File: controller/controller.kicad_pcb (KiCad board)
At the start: 4 copper layers, 93 x 39 mm, 132 parts, among them J1 Conn_01x14, J2 Conn_01x14, J3 Conn_01x14, J4 Conn_01x14, J5 Conn_01x14, J6 USB_C_Receptacle_USB2.0_16P, J7 USB_C_Receptacle_USB2.0_16P, J8 GRPB072VWQS-RC, J9 Conn_01x03_Pin, U1 STM32G474RCTx, U10 PI5C3257, U11 QSBT40-7-F, U12 QSBT40-7-F, U13 QSBT40-7-F, U2 LM5168, U3 TLV76133DCY, U4 TLV76150DCY, U5 ECMF02-2AMX6, U6 ESP32-C6-WROOM-1, U7 ECMF02-2AMX6, U8 PI5C3257, U9 PY32F002AA15M

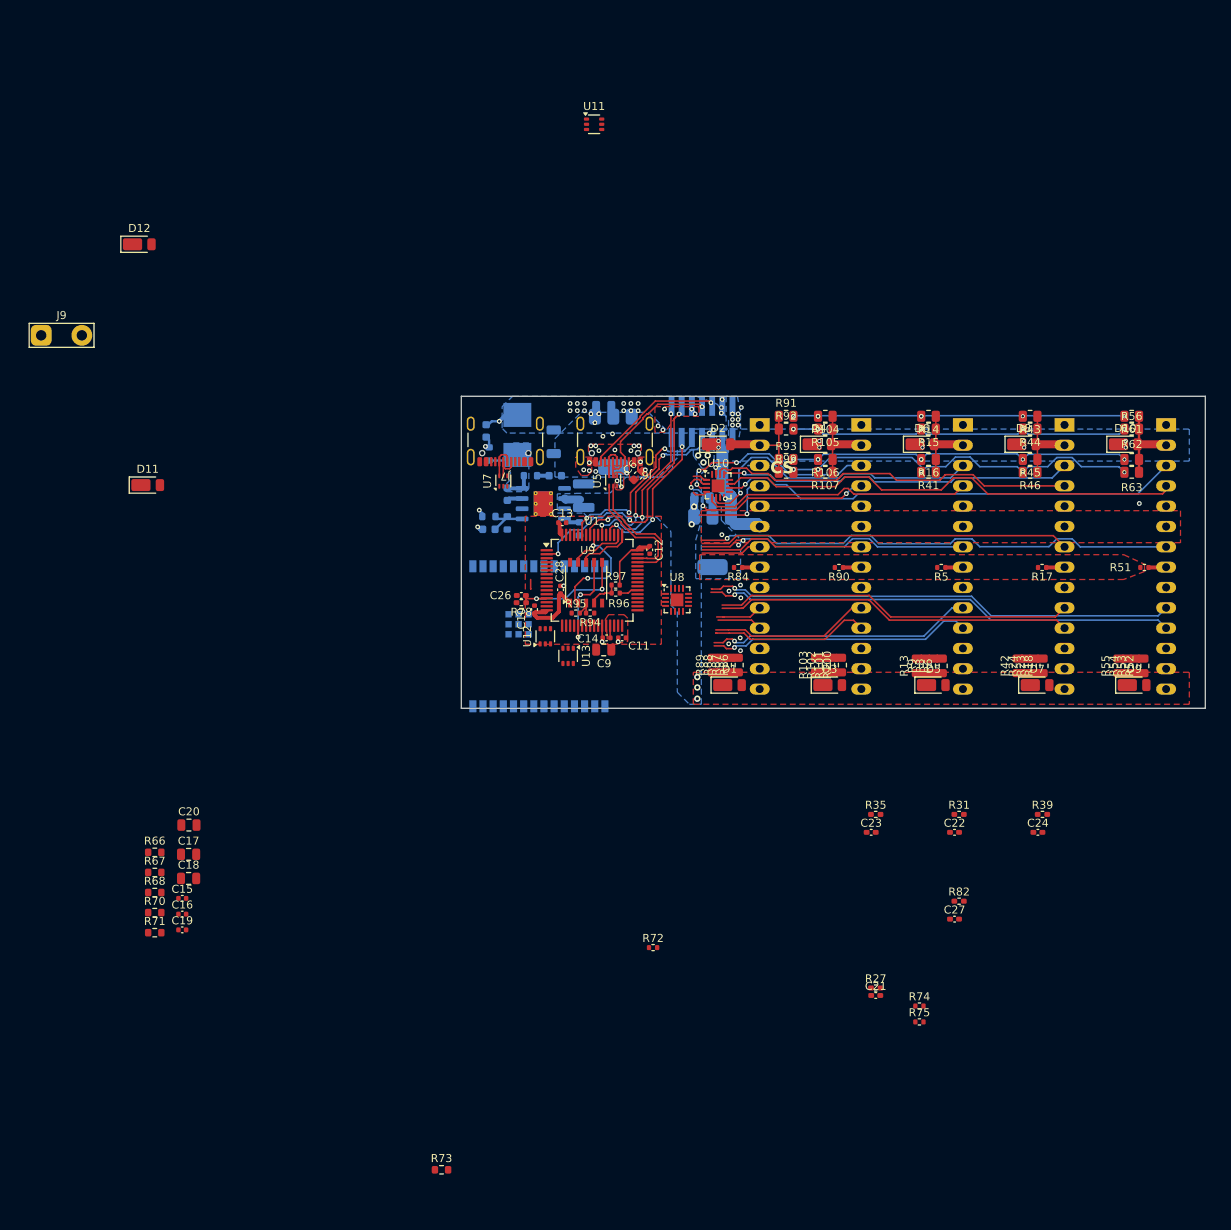
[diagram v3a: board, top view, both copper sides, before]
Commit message: Controller move DC/DC to between HB4 and HB5
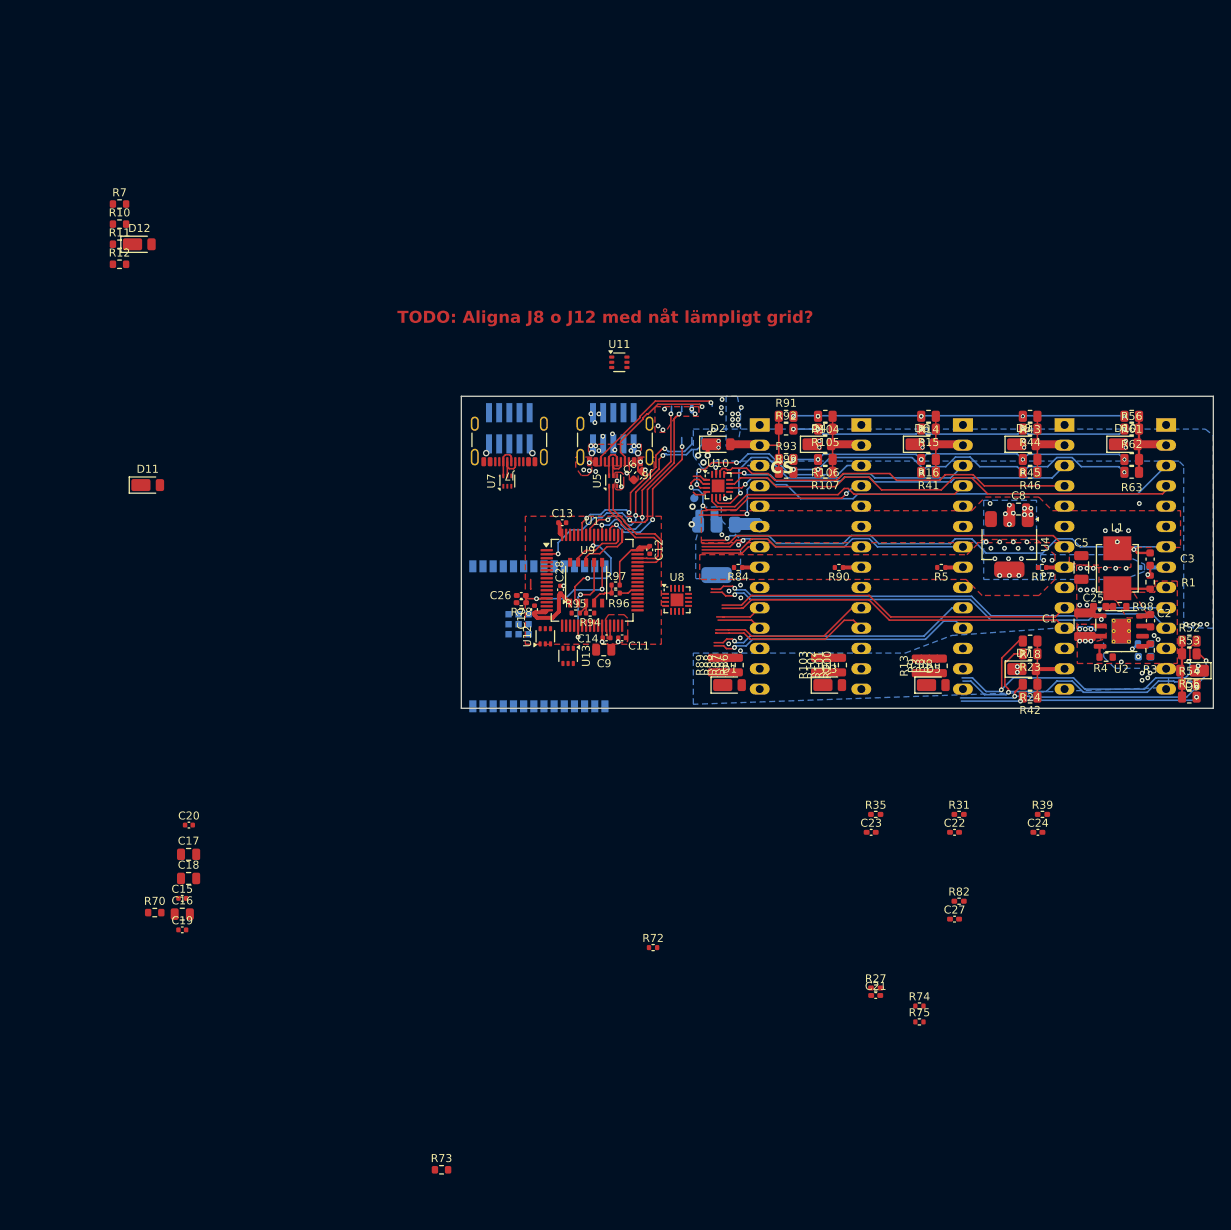
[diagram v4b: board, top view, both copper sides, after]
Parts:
- removed J9: Conn_01x03_Pin, TestPoint:TestPoint_2Pads_Pitch5.08mm_Drill1.3mm
- removed R66, R67, R68: 10k, Resistor_SMD:R_0603_1608Metric
- removed R71: 1k, Resistor_SMD:R_0603_1608Metric
- added J12: GRPB072VWQS-RC, Connector_PinHeader_1.27mm:PinHeader_2x05_P1.27mm_Vertical_SMD, B.Cu at (83.0, 69.0)
- added R10: 10k, Resistor_SMD:R_0603_1608Metric, F.Cu at (34.3, 43.5)
- added R11: 10k, Resistor_SMD:R_0603_1608Metric, F.Cu at (34.3, 46.0)
- added R12: 1k, Resistor_SMD:R_0603_1608Metric, F.Cu at (34.3, 48.5)
- added R7: 10k, Resistor_SMD:R_0603_1608Metric, F.Cu at (34.3, 41.0)
- C1, C2, C25, C3, C5, C8, R1, R3, R4, R98, U4: moved to F.Cu
- C16: value 100nF -> 10uF; footprint Capacitor_SMD:C_0402_1005Metric -> Capacitor_SMD:C_0805_2012Metric
- C20: value 10uF -> 100nF; footprint Capacitor_SMD:C_0805_2012Metric -> Capacitor_SMD:C_0402_1005Metric
- J8: footprint Connector_PinHeader_1.27mm:PinHeader_2x07_P1.27mm_Vertical_SMD -> Connector_PinHeader_1.27mm:PinHeader_2x05_P1.27mm_Vertical_SMD
- L1: value 180uH 630mOhm, duger LQH55DN151M03L? -> duger CLF7045NIT-151M-D?; moved to F.Cu
- R51: moved to B.Cu
- U2: value LM5168 -> LM5169PDDAR; moved to F.Cu
- moved C3 84.5 mm to (163.1, 85.4)
- moved R1 84.2 mm to (163.1, 88.2)
- moved C4 83.5 mm to (162.4, 97.6)
- moved R2 83.5 mm to (162.4, 96.0)
- moved C2 81.9 mm to (163.2, 93.1)
- moved R3 81.9 mm to (163.1, 96.8)
- moved L1 76.8 mm to (159.0, 86.5)
- moved R98 75.5 mm to (159.3, 91.3), turned to 180 degrees
- moved U2 74.0 mm to (159.5, 94.4), turned to 0 degrees
- moved C25 70.0 mm to (156.8, 91.3), turned to 180 degrees
- moved C5 67.8 mm to (154.5, 86.4)
- moved R4 67.8 mm to (157.6, 97.6), turned to 0 degrees
- moved C1 64.7 mm to (154.9, 93.6)
- moved C8 39.6 mm to (146.7, 79.1), turned to 0 degrees
- moved U4 37.1 mm to (145.5, 83.5)
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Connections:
- net ESP_USB_D+ renamed /ESP_USB_D+
- net ESP_USB_D- renamed /ESP_USB_D-
- net Net-(D11-A) renamed /VBUS1
- net Net-(D12-A) renamed /VBUS2
- C15 pad 1: Net-(U6-EN/CHIP_PU) -> +3V3
- C20 pad 1: +3V3 -> Net-(U6-EN/CHIP_PU)
- J8 pad 10: +3V3 -> 6-18V
- J8 pad 3: 6-18V -> Earth
- J8 pad 7: /CC2_MCU -> Earth
- J8 pad 9: /CC1_MCU -> +3V3
- U2 pad 6: unconnected-(U2-PGOOD-Pad6) -> Earth
- U6 pad 18: /STM32_BOOT0 -> /STM32_NRST_TO_ESP
- U6 pad 19: /STM32_NRST_TO_ESP -> /STM32_BOOT0
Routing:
- net FB_A_FULL: track 58.2 -> 101.8 mm, vias 7 -> 9
- net FB_B_FULL: track 55.2 -> 98.5 mm, vias 7 -> 9
- net FB_C_FULL: track 43.0 -> 75.1 mm, vias 5 -> 7
- net FB_D_FULL: track 46.3 -> 76.2 mm, vias 5 -> 7
- net /hb-card4/FB_x_FULL_HI: track 0.08 -> 10.7 mm
- net 6-18V: track 30.8 -> 21.0 mm, vias 14 -> 10
- net /hb-card5/FB_x_FULL_HI: track 0.08 -> 7.08 mm
- net Net-(U2-FB): track 5.66 -> 0.00 mm
- net Net-(U2-SW): track 7.37 -> 4.12 mm
- net +5V: track 2.49 -> 0.00 mm, vias 0 -> 22
- net Net-(U2-BST): track 1.94 -> 0.00 mm
- net Net-(C3-Pad2): track 13.9 -> 12.4 mm
- net Earth: track 5.22 -> 3.72 mm, vias 34 -> 46
- net Logic DC/DC in: track 2.99 -> 1.89 mm, vias 16 -> 31
- net Net-(U2-RON): track 2.04 -> 1.37 mm
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- added copper zone on In2.Cu, net Logic DC/DC in
- added copper zone on F.Cu, net Net-(U2-SW)
- removed copper zone on B.Cu, net 6-18V
- removed copper zone on In2.Cu, net 6-18V
- removed copper zone on B.Cu, net Net-(U2-SW)
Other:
- board size 93 x 39 mm -> 94 x 39 mm
- board text added: "TODO: Aligna J8 o J12 med nåt lämpligt grid?"
- board text added: "USB PD expansion PCB"

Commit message: Controller - Some smaller changes, add 3d models etc
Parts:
- added J9: GRPB072VWQS-RC, Connector_PinHeader_1.27mm:PinHeader_2x05_P1.27mm_Vertical_SMD, B.Cu at (104.7, 69.0)
- C15, C16, C17, C18: moved to B.Cu
- moved R73 74.7 mm to (83.4, 87.5)
- moved D12 69.9 mm to (102.4, 69.9), turned to -90 degrees
- moved C16 61.4 mm to (82.7, 83.6)
- moved R75 59.3 mm to (95.6, 98.2), turned to 180 degrees
- moved C18 59.1 mm to (82.7, 81.6)
- moved R74 57.1 mm to (95.6, 99.2), turned to 180 degrees
- moved C15 57.1 mm to (79.0, 84.2), turned to 180 degrees
- moved C17 53.8 mm to (79.2, 82.6), turned to 180 degrees
- moved D11 52.3 mm to (89.6, 69.2), turned to -90 degrees
- moved R12 50.5 mm to (64.6, 88.9)
- moved R7 50.5 mm to (64.6, 81.4)
- moved R10 50.5 mm to (64.6, 83.9)
- moved R11 50.5 mm to (64.6, 86.4)
- moved R72 44.8 mm to (101.3, 89.1), turned to -90 degrees
- moved R27 21.4 mm to (137.6, 119.5)
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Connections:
- net /HI_4 renamed HI_4
- net /HI_5 renamed HI_5
- net /LI_4 renamed LI_4
- net /LI_5 renamed LI_5
- J7 pad A5: unconnected-(J7-CC1-PadA5) -> /OTHER_USB_CC1
- J7 pad B5: unconnected-(J7-CC2-PadB5) -> /OTHER_USB_CC2
- U1 pad 10: Net-(U1-PC2) -> /PC2
- U1 pad 11: ADC12_IN9 -> /NTC_2
- U1 pad 22: /NTC_5 -> unconnected-(U1-PC4-Pad22)
- U1 pad 26: ADC2_IN12 -> /PB2
- U1 pad 5: /NTC_2 -> /NTC_4
- U1 pad 53: unconnected-(U1-PC11-Pad53) -> /PC11
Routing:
- net /STM32_TX: track 13.6 -> 28.1 mm, vias 2 -> 3
- net /STM32_RX: track 0.00 -> 12.8 mm, vias 0 -> 1
- net /CC2: track 17.9 -> 7.52 mm, vias 1 -> 0
- net /CC1: track 15.7 -> 6.73 mm, vias 3 -> 0
- net /~{EN_CC}: track 32.1 -> 23.8 mm, vias 3 -> 2
- net +3V3: track 20.1 -> 27.5 mm
- net /PA4: track 0.00 -> 7.11 mm
- net /CC2_MCU: track 23.9 -> 16.8 mm, vias 3 -> 2
- net /FRS: track 23.6 -> 16.7 mm, vias 3 -> 2
- net /CC1_MCU: track 22.9 -> 16.7 mm, vias 3 -> 2
- net /PA5: track 0.00 -> 4.79 mm
- net /~{EN_VCONN}: track 19.2 -> 16.4 mm, vias 3 -> 2
- net /hb-card5/FB_x_FULL_HI: track 7.08 -> 8.87 mm
- net Earth: vias 46 -> 53
- net /VBUS1: vias 17 -> 14

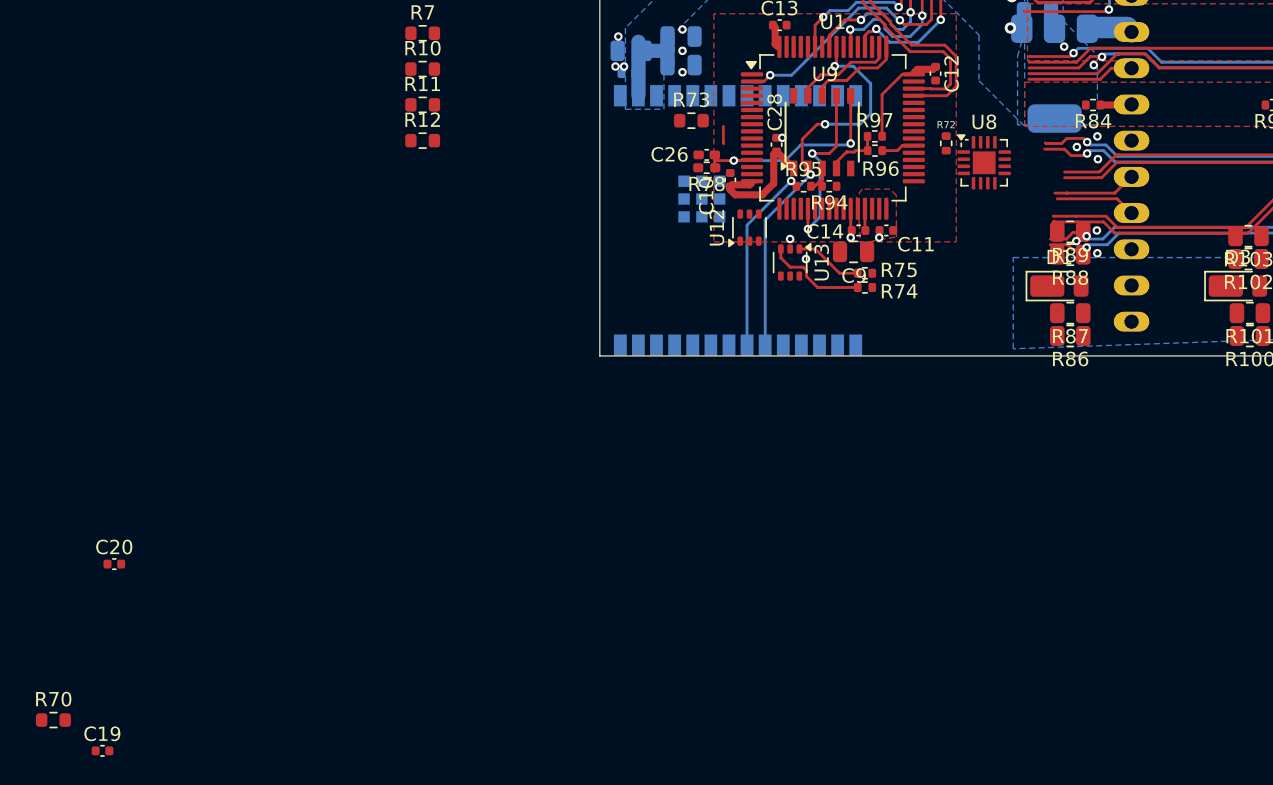
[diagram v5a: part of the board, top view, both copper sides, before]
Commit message: Controller and firwmare most pins in sync
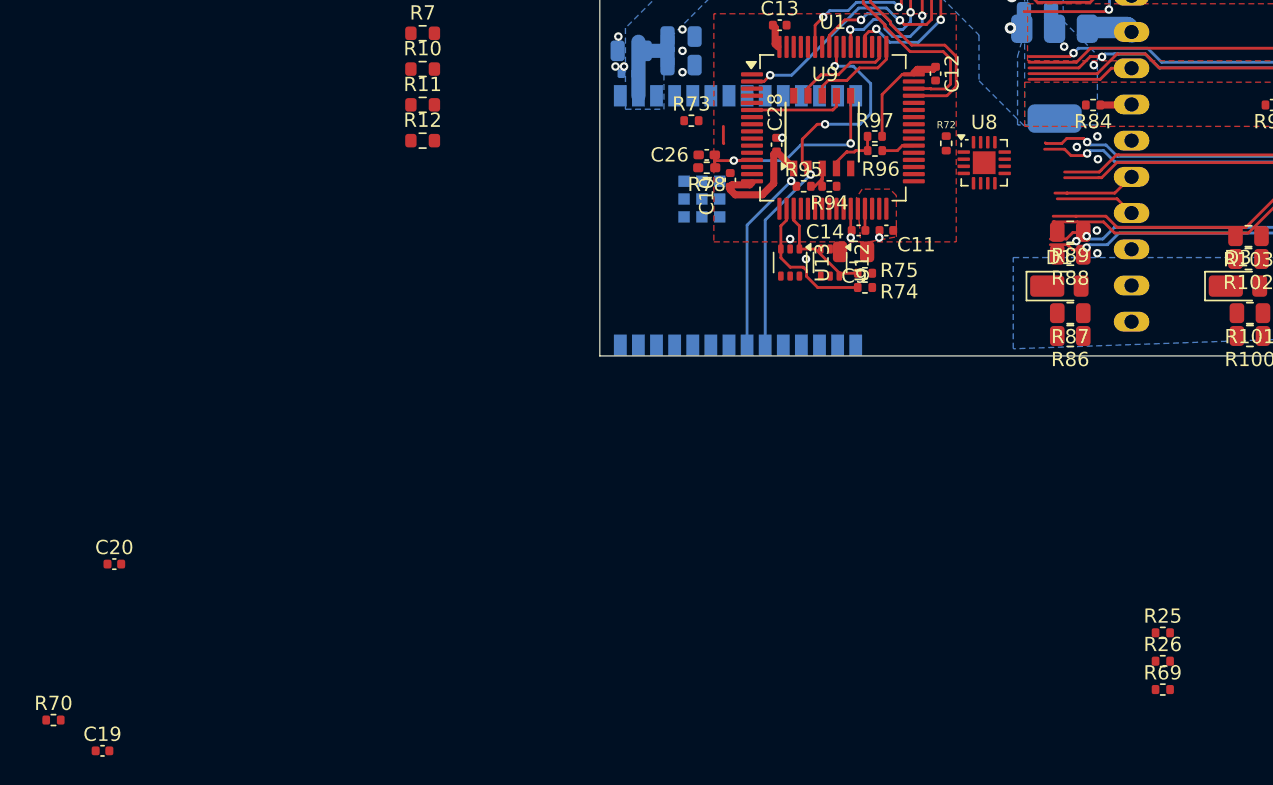
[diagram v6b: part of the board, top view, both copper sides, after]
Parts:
- added R25: 0R, Resistor_SMD:R_0402_1005Metric, F.Cu at (116.5, 123.4)
- added R26: 0R, Resistor_SMD:R_0402_1005Metric, F.Cu at (116.5, 125.4)
- added R69: 10k, Resistor_SMD:R_0402_1005Metric, F.Cu at (116.5, 127.4)
- R70, R73: footprint Resistor_SMD:R_0603_1608Metric -> Resistor_SMD:R_0402_1005Metric
- moved U12 6.16 mm to (93.2, 97.5), turned to -90 degrees
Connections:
- net HRTIM1_EEV3 renamed /pwm_led2
- net HRTIM1_EEV5 renamed /pwm_led3
- net HRTIM1_EEV6 renamed /pwm_led1
- net HRTIM1_FLT3 renamed /pwm_led4
- U1 pad 13: FB_A_FULL -> /Current_sense_4
- U1 pad 17: /Current_sense_1B -> /pwm_led5 pot2
- U1 pad 21: FB_B_FULL -> /Current_sense_5
- U1 pad 22: unconnected-(U1-PC4-Pad22) -> FB_D_FULL
- U1 pad 25: /Current_sense_3 -> /pwm_led6 pot3
- U1 pad 33: /Current_sense_? -> /Current_sense_2
- U1 pad 36: /Current_sense_2 -> /Current_sense_3
- U1 pad 6: ADC2_IN10 -> FB_B_FULL
- U1 pad 9: FB_D_FULL -> /Current_sense_1B
- U8 pad 10: LI_5 -> LI_4
- U8 pad 13: HI_5 -> HI_4
- U8 pad 3: HI_4 -> HI_5
- U8 pad 6: LI_4 -> LI_5
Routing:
- net FB_B_FULL: track 98.9 -> 93.0 mm, vias 9 -> 7
- net /PA5: track 4.79 -> 7.78 mm
- net /PA4: track 7.11 -> 10.1 mm

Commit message: Controller - some more changes
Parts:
- added C29: 10nF, Capacitor_SMD:C_0402_1005Metric, F.Cu at (132.6, 158.9)
- added C30: 10nF, Capacitor_SMD:C_0402_1005Metric, F.Cu at (132.6, 160.9)
- added C31: 10nF, Capacitor_SMD:C_0402_1005Metric, F.Cu at (132.6, 162.9)
- added C32: 10nF, Capacitor_SMD:C_0402_1005Metric, F.Cu at (132.6, 164.8)
- added C33: 10nF, Capacitor_SMD:C_0402_1005Metric, F.Cu at (123.7, 151.0)
- added C34: 10nF, Capacitor_SMD:C_0402_1005Metric, F.Cu at (132.6, 166.8)
- added C35: 10nF, Capacitor_SMD:C_0402_1005Metric, F.Cu at (132.6, 151.0)
- added C38: 10nF, Capacitor_SMD:C_0402_1005Metric, F.Cu at (114.8, 151.0)
- added C39: 10nF, Capacitor_SMD:C_0402_1005Metric, F.Cu at (114.8, 158.9)
- added C40: 10nF, Capacitor_SMD:C_0402_1005Metric, F.Cu at (123.7, 158.9)
- added C41: 10nF, Capacitor_SMD:C_0402_1005Metric, F.Cu at (123.7, 153.0)
- added C42: 10nF, Capacitor_SMD:C_0402_1005Metric, F.Cu at (132.6, 153.0)
- added C43: 10nF, Capacitor_SMD:C_0402_1005Metric, F.Cu at (114.8, 153.0)
- added C44: 10nF, Capacitor_SMD:C_0402_1005Metric, F.Cu at (114.8, 160.9)
- added C45: 10nF, Capacitor_SMD:C_0402_1005Metric, F.Cu at (123.7, 160.9)
- added C46: 10nF, Capacitor_SMD:C_0402_1005Metric, F.Cu at (123.7, 154.9)
- added C47: 10nF, Capacitor_SMD:C_0402_1005Metric, F.Cu at (132.6, 154.9)
- added C48: 10nF, Capacitor_SMD:C_0402_1005Metric, F.Cu at (114.8, 154.9)
- added C49: 10nF, Capacitor_SMD:C_0402_1005Metric, F.Cu at (114.8, 162.9)
- added C50: 10nF, Capacitor_SMD:C_0402_1005Metric, F.Cu at (123.7, 162.9)
- added C51: 1nF 100VDC, Capacitor_SMD:C_0603_1608Metric, F.Cu at (117.1, 99.1)
- added C52: 1nF 100VDC, Capacitor_SMD:C_0603_1608Metric, F.Cu at (142.5, 99.1)
- added C53: 1nF 100VDC, Capacitor_SMD:C_0603_1608Metric, F.Cu at (155.2, 99.1)
- added C54: 1nF 100VDC, Capacitor_SMD:C_0603_1608Metric, B.Cu at (168.1, 99.1)
- added C55: 1nF 100VDC, Capacitor_SMD:C_0603_1608Metric, F.Cu at (129.8, 99.1)
- added C56: 1nF 100VDC, Capacitor_SMD:C_0603_1608Metric, F.Cu at (117.1, 71.1)
- added C57: 1nF 100VDC, Capacitor_SMD:C_0603_1608Metric, F.Cu at (142.5, 71.1)
- added C58: 1nF 100VDC, Capacitor_SMD:C_0603_1608Metric, F.Cu at (155.2, 71.1)
- added C59: 1nF 100VDC, Capacitor_SMD:C_0603_1608Metric, F.Cu at (167.7, 71.1)
- added C60: 1nF 100VDC, Capacitor_SMD:C_0603_1608Metric, F.Cu at (129.8, 71.2)
- added R28: 0R, Resistor_SMD:R_0402_1005Metric, F.Cu at (135.5, 158.9)
- added R29: 0R, Resistor_SMD:R_0402_1005Metric, F.Cu at (135.5, 160.9)
- added R30: 0R, Resistor_SMD:R_0402_1005Metric, F.Cu at (135.5, 162.9)
- added R32: 0R, Resistor_SMD:R_0402_1005Metric, F.Cu at (135.5, 164.9)
- C21, C22, C23, C24, C26, C27: value 100nF -> 10nF
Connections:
- U1 pad 23: ADC2_IN11 -> /pwm_led7
